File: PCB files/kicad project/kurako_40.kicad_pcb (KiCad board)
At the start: 2 copper layers, 226 x 76.5 mm, 114 parts, among them J1 conn, P1 USB_C_Plug_USB2.0, SW1 TAB, SW10 S, SW11 X, SW12 PROG, SW13 E, SW14 D, SW15 C, SW16 ALT, SW17 R, SW18 F, SW19 V, SW2 ESC, SW20 SPACE, SW21 T, SW22 G, SW23 B, SW24 Y, SW25 H, SW26 N, SW27 LOWER, SW28 U, SW29 J, SW3 SHIFT, SW30 M, SW31 RAISE, SW32 I, SW33 K, SW34 ,, SW35 /, SW36 O, SW37 L, SW38 ., SW39 LEFT, SW4 CTRL, SW40 P, SW41 ;, SW42 UP, SW43 DOWN, SW44 BKSP, SW45 ', SW46 ENTER, SW47 RIGHT, SW48 SW_SPST, SW5 Q, SW6 A, SW7 Z, SW8 WIN, SW9 W, U1 ATmega32U4-AU, Y1 16 Mhz

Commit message: bad keyswitch placements
prior rev had bad switch placement, updated and gave the board a rev number
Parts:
- moved SW42 0.10 mm to (240.0, 108.0)
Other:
- board text added: "kurako_40 Rev 1.1 Nathan Steward"
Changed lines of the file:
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@@
   (general
     (thickness 1.6)
-    (drawings 18)
+    (drawings 19)
     (tracks 1134)
     (zones 0)
@@
     )
   )
-  (module keyswitches:Kailh_socket (layer F.Cu)
+  (module keyswitches:Kailh_socket locked (layer F.Cu)
     (at 126 70 180)
     (descr "MX-style keyswitch with Kailh socket mount")
@@
     )
   )
-  (module keyswitches:Kailh_socket (layer F.Cu)
+  (module keyswitches:Kailh_socket locked (layer F.Cu)
     (at 126 108 180)
     (descr "MX-style keyswitch with Kailh socket mount")
@@
     )
   )
-  (module keyswitches:Kailh_socket (layer F.Cu)
+  (module keyswitches:Kailh_socket locked (layer F.Cu)
     (at 164 70 180)
     (descr "MX-style keyswitch with Kailh socket mount")
@@
     )
   )
-  (module keyswitches:Kailh_socket (layer F.Cu)
+  (module keyswitches:Kailh_socket locked (layer F.Cu)
     (at 202 108 180)
     (descr "MX-style keyswitch with Kailh socket mount")
@@
     )
   )
-  (module keyswitches:Kailh_socket (layer F.Cu)
+  (module keyswitches:Kailh_socket locked (layer F.Cu)
     (at 202 89 180)
     (descr "MX-style keyswitch with Kailh socket mount")
@@
     )
   )
-  (module keyswitches:Kailh_socket (layer F.Cu)
+  (module keyswitches:Kailh_socket locked (layer F.Cu)
     (at 202 70 180)
     (descr "MX-style keyswitch with Kailh socket mount")
@@
     )
   )
-  (module keyswitches:Kailh_socket (layer F.Cu)
+  (module keyswitches:Kailh_socket locked (layer F.Cu)
     (at 183 127 180)
     (descr "MX-style keyswitch with Kailh socket mount")
@@
     )
   )
-  (module keyswitches:Kailh_socket (layer F.Cu)
+  (module keyswitches:Kailh_socket locked (layer F.Cu)
     (at 183 108 180)
     (descr "MX-style keyswitch with Kailh socket mount")
@@
     )
   )
-  (module keyswitches:Kailh_socket (layer F.Cu)
+  (module keyswitches:Kailh_socket locked (layer F.Cu)
     (at 183 89 180)
     (descr "MX-style keyswitch with Kailh socket mount")
@@
     )
   )
-  (module keyswitches:Kailh_socket (layer F.Cu)
+  (module keyswitches:Kailh_socket locked (layer F.Cu)
     (at 183 70 180)
     (descr "MX-style keyswitch with Kailh socket mount")
@@
     )
   )
-  (module keyswitches:Kailh_socket (layer F.Cu)
+  (module keyswitches:Kailh_socket locked (layer F.Cu)
     (at 164 127 180)
     (descr "MX-style keyswitch with Kailh socket mount")
@@
     )
   )
-  (module keyswitches:Kailh_socket (layer F.Cu)
+  (module keyswitches:Kailh_socket locked (layer F.Cu)
     (at 164 108 180)
     (descr "MX-style keyswitch with Kailh socket mount")
@@
     )
   )
-  (module keyswitches:Kailh_socket (layer F.Cu)
+  (module keyswitches:Kailh_socket locked (layer F.Cu)
     (at 145 108 180)
     (descr "MX-style keyswitch with Kailh socket mount")
@@
     )
   )
-  (module keyswitches:Kailh_socket (layer F.Cu)
+  (module keyswitches:Kailh_socket locked (layer F.Cu)
     (at 202 127 180)
     (descr "MX-style keyswitch with Kailh socket mount")
@@
     )
   )
-  (module keyswitches:Kailh_socket (layer F.Cu)
+  (module keyswitches:Kailh_socket locked (layer F.Cu)
     (at 221 108 180)
     (descr "MX-style keyswitch with Kailh socket mount")
@@
     )
   )
-  (module keyswitches:Kailh_socket (layer F.Cu)
+  (module keyswitches:Kailh_socket locked (layer F.Cu)
     (at 221 127 180)
     (descr "MX-style keyswitch with Kailh socket mount")
@@
     )
   )
-  (module keyswitches:Kailh_socket (layer F.Cu)
+  (module keyswitches:Kailh_socket locked (layer F.Cu)
     (at 240 70 180)
     (descr "MX-style keyswitch with Kailh socket mount")
@@
     )
   )
-  (module keyswitches:Kailh_socket (layer F.Cu)
+  (module keyswitches:Kailh_socket locked (layer F.Cu)
     (at 240 89 180)
     (descr "MX-style keyswitch with Kailh socket mount")
@@
     )
   )
-  (module keyswitches:Kailh_socket (layer F.Cu)
-    (at 240 108.1 180)
+  (module keyswitches:Kailh_socket locked (layer F.Cu)
+    (at 240 108 180)
     (descr "MX-style keyswitch with Kailh socket mount")
     (tags MX,cherry,gateron,kailh,pg1511,socket)
@@
     )
   )
-  (module keyswitches:Kailh_socket (layer F.Cu)
+  (module keyswitches:Kailh_socket locked (layer F.Cu)
     (at 240 127 180)
     (descr "MX-style keyswitch with Kailh socket mount")
@@
     )
   )
-  (module keyswitches:Kailh_socket (layer F.Cu)
+  (module keyswitches:Kailh_socket locked (layer F.Cu)
     (at 259 70 180)
     (descr "MX-style keyswitch with Kailh socket mount")
@@
     )
   )
-  (module keyswitches:Kailh_socket (layer F.Cu)
+  (module keyswitches:Kailh_socket locked (layer F.Cu)
     (at 259 89 180)
     (descr "MX-style keyswitch with Kailh socket mount")
@@
     )
   )
-  (module keyswitches:Kailh_socket (layer F.Cu)
+  (module keyswitches:Kailh_socket locked (layer F.Cu)
     (at 259 108 180)
     (descr "MX-style keyswitch with Kailh socket mount")
@@
     )
   )
-  (module keyswitches:Kailh_socket (layer F.Cu)
+  (module keyswitches:Kailh_socket locked (layer F.Cu)
     (at 259 127 180)
     (descr "MX-style keyswitch with Kailh socket mount")
@@
     )
   )
-  (module keyswitches:Kailh_socket (layer F.Cu)
+  (module keyswitches:Kailh_socket locked (layer F.Cu)
     (at 88 127 180)
     (descr "MX-style keyswitch with Kailh socket mount")
@@
     )
   )
-  (module keyswitches:Kailh_socket (layer F.Cu)
+  (module keyswitches:Kailh_socket locked (layer F.Cu)
     (at 221 70 180)
     (descr "MX-style keyswitch with Kailh socket mount")
@@
     )
   )
-  (module keyswitches:Kailh_socket (layer F.Cu)
+  (module keyswitches:Kailh_socket locked (layer F.Cu)
     (at 88 89 180)
     (descr "MX-style keyswitch with Kailh socket mount")
@@
     )
   )
-  (module keyswitches:Kailh_socket (layer F.Cu)
+  (module keyswitches:Kailh_socket locked (layer F.Cu)
     (at 88 70 180)
     (descr "MX-style keyswitch with Kailh socket mount")
@@
     )
   )
-  (module keyswitches:Kailh_socket (layer F.Cu)
+  (module keyswitches:Kailh_socket locked (layer F.Cu)
     (at 69 127 180)
     (descr "MX-style keyswitch with Kailh socket mount")
@@
     )
   )
-  (module keyswitches:Kailh_socket (layer F.Cu)
+  (module keyswitches:Kailh_socket locked (layer F.Cu)
     (at 69 108 180)
     (descr "MX-style keyswitch with Kailh socket mount")
@@
     )
   )
-  (module keyswitches:Kailh_socket (layer F.Cu)
+  (module keyswitches:Kailh_socket locked (layer F.Cu)
     (at 69 89 180)
     (descr "MX-style keyswitch with Kailh socket mount")
@@
     )
   )
-  (module keyswitches:Kailh_socket (layer F.Cu)
+  (module keyswitches:Kailh_socket locked (layer F.Cu)
     (at 69 70 180)
     (descr "MX-style keyswitch with Kailh socket mount")
@@
     )
   )
-  (module keyswitches:Kailh_socket (layer F.Cu)
+  (module keyswitches:Kailh_socket locked (layer F.Cu)
     (at 50 127 180)
     (descr "MX-style keyswitch with Kailh socket mount")
@@
     )
   )
-  (module keyswitches:Kailh_socket (layer F.Cu)
+  (module keyswitches:Kailh_socket locked (layer F.Cu)
     (at 50 108 180)
     (descr "MX-style keyswitch with Kailh socket mount")
@@
     )
   )
-  (module keyswitches:Kailh_socket (layer F.Cu)
+  (module keyswitches:Kailh_socket locked (layer F.Cu)
     (at 50 89 180)
     (descr "MX-style keyswitch with Kailh socket mount")
@@
     )
   )
-  (module keyswitches:Kailh_socket (layer F.Cu)
+  (module keyswitches:Kailh_socket locked (layer F.Cu)
     (at 164 89 180)
     (descr "MX-style keyswitch with Kailh socket mount")
@@
     )
   )
-  (module keyswitches:Kailh_socket (layer F.Cu)
+  (module keyswitches:Kailh_socket locked (layer F.Cu)
     (at 107 70 180)
     (descr "MX-style keyswitch with Kailh socket mount")
@@
     )
   )
-  (module keyswitches:Kailh_socket (layer F.Cu)
+  (module keyswitches:Kailh_socket locked (layer F.Cu)
     (at 107 89 180)
     (descr "MX-style keyswitch with Kailh socket mount")
@@
     )
   )
-  (module keyswitches:Kailh_socket (layer F.Cu)
+  (module keyswitches:Kailh_socket locked (layer F.Cu)
     (at 107 108)
     (descr "MX-style keyswitch with Kailh socket mount")
@@
     )
   )
-  (module keyswitches:Kailh_socket (layer F.Cu)
+  (module keyswitches:Kailh_socket locked (layer F.Cu)
     (at 107 127 180)
     (descr "MX-style keyswitch with Kailh socket mount")
@@
     )
   )
-  (module keyswitches:Kailh_socket (layer F.Cu)
+  (module keyswitches:Kailh_socket locked (layer F.Cu)
     (at 126 89 180)
     (descr "MX-style keyswitch with Kailh socket mount")
@@
     )
   )
-  (module keyswitches:Kailh_socket (layer F.Cu)
+  (module keyswitches:Kailh_socket locked (layer F.Cu)
     (at 135.5 127 180)
     (descr "MX-style keyswitch with Kailh socket mount")
@@
     )
   )
-  (module keyswitches:Kailh_socket (layer F.Cu)
+  (module keyswitches:Kailh_socket locked (layer F.Cu)
     (at 145 70 180)
     (descr "MX-style keyswitch with Kailh socket mount")
@@
     )
   )
-  (module keyswitches:Kailh_socket (layer F.Cu)
+  (module keyswitches:Kailh_socket locked (layer F.Cu)
     (at 145 89 180)
     (descr "MX-style keyswitch with Kailh socket mount")
@@
     )
   )
-  (module keyswitches:Kailh_socket (layer F.Cu)
+  (module keyswitches:Kailh_socket locked (layer F.Cu)
     (at 221 89 180)
     (descr "MX-style keyswitch with Kailh socket mount")
@@
     )
   )
-  (module keyswitches:Kailh_socket (layer F.Cu)
+  (module keyswitches:Kailh_socket locked (layer F.Cu)
     (at 88 108)
     (descr "MX-style keyswitch with Kailh socket mount")
@@
     )
   )
-  (module Connector_USB:USB_C_Receptacle_Amphenol_12401610E4-2A (layer B.Cu)
+  (module Connector_USB:USB_C_Receptacle_Amphenol_12401610E4-2A locked (layer B.Cu)
     (at 78.5 62.5)
     (descr "USB TYPE C, RA RCPT PCB, SMT, https://www.amphenolcanada.com/StockAvailabilityPrice.aspx?From=&PartNum=12401610E4%7e2A")
@@
     (pad "" np_thru_hole circle (at -11.9 6.985) (size 3.048 3.048) (drill 3.048) (layers *.Cu *.Mask))
   )
+  (gr_text "kurako_40 Rev 1.1\nNathan Steward" (at 59.5 65) (layer B.SilkS)
+    (effects (font (size 1.5 1.5) (thickness 0.3)) (justify mirror))
+  )
   (gr_text SCK (at 62.25 101.25) (layer B.SilkS)

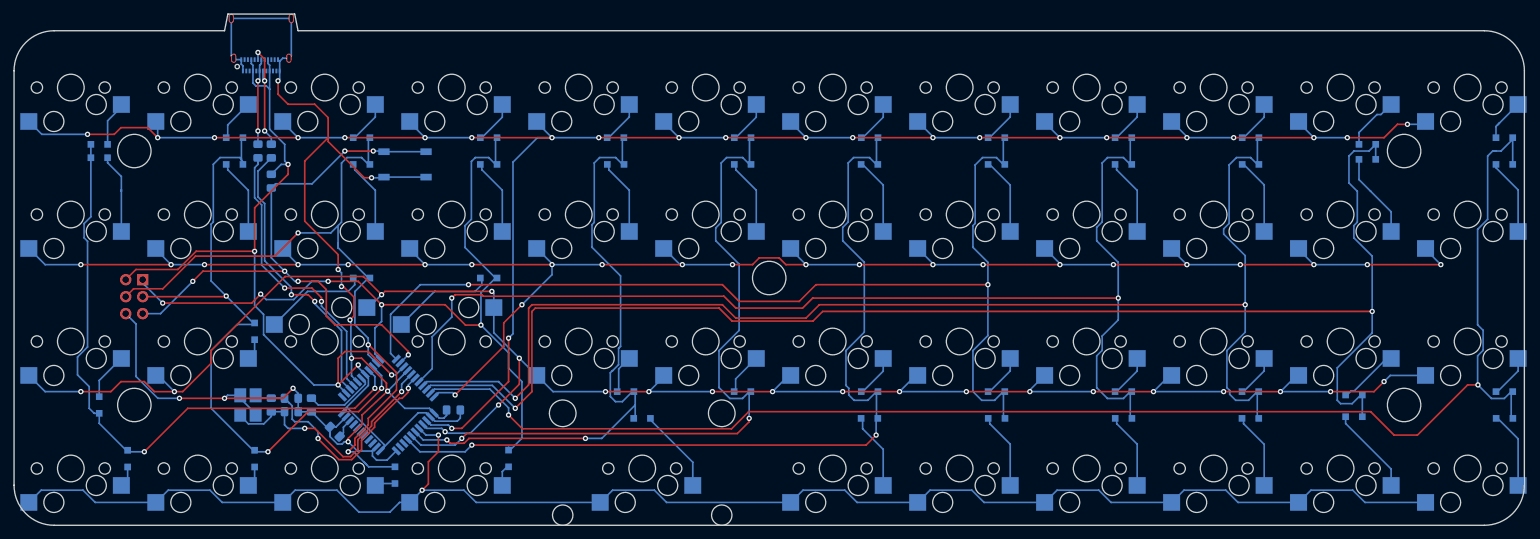
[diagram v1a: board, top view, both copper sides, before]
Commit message: board rev changes v1.2
updated schematic from SOD323 diodes to SOD80 due to cost savings and ease of soldering. added ground fill on top and bottom
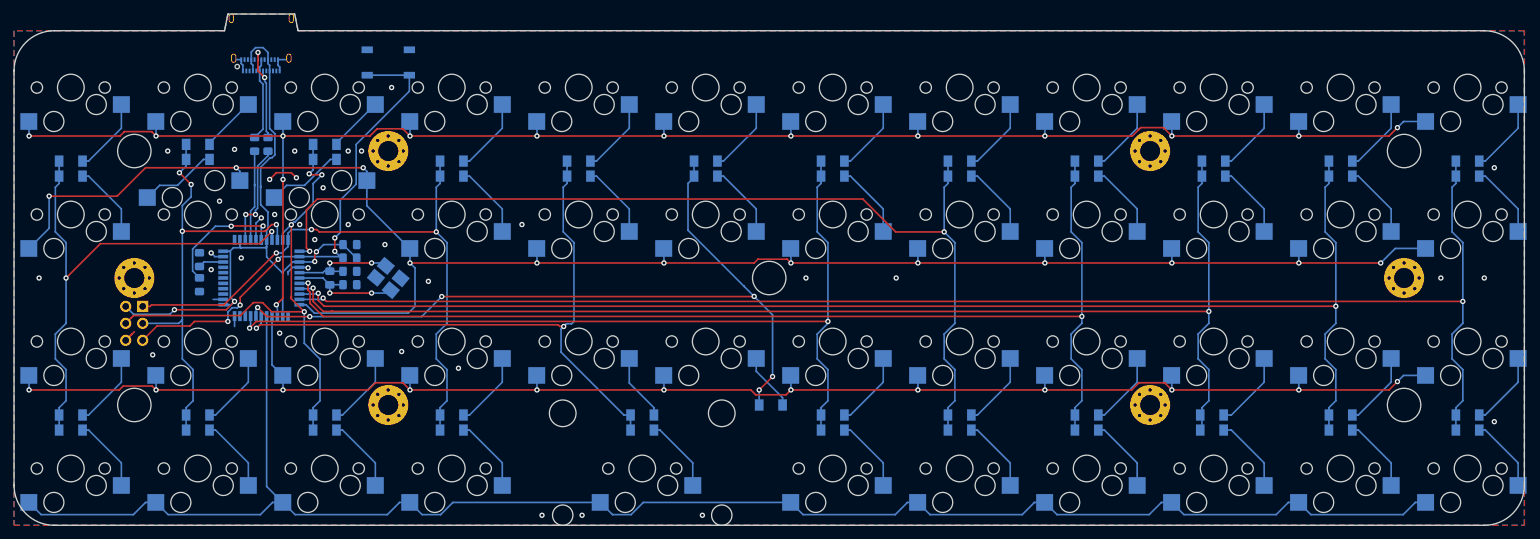
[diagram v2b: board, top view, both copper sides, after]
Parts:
- added ?: MountingHole_3mm_Pad_Via, MountingHole:MountingHole_3mm_Pad_Via, F.Cu at (249.5, 98.5)
- added ?: MountingHole_3mm_Pad_Via, MountingHole:MountingHole_3mm_Pad_Via, F.Cu at (211.5, 117.5)
- added ?: MountingHole_3mm_Pad_Via, MountingHole:MountingHole_3mm_Pad_Via, F.Cu at (211.5, 79.5)
- added ?: MountingHole_3mm_Pad_Via, MountingHole:MountingHole_3mm_Pad_Via, F.Cu at (97.5, 117.5)
- added ?: MountingHole_3mm_Pad_Via, MountingHole:MountingHole_3mm_Pad_Via, F.Cu at (97.5, 79.5)
- added ?: MountingHole_3mm_Pad_Via, MountingHole:MountingHole_3mm_Pad_Via, F.Cu at (59.5, 98.5)
- added G***: LOGO, silkscreen library:pjmeme_edit, B.Cu at (233.0, 98.4)
- D1, D10, D11, D12, D13, D14, D15, D16, D17, D18, D19, D2, D20, D21, D22, D23, D24, D25, D26, D27, D28, D29, D3, D30, D31, D32, D33, D34, D35, D36, D37, D38, D39, D4, D40, D41, D42, D43, D44, D45, D46, D47, D5, D6, D7, D8, D9: footprint Diode_SMD:D_SOD-323_HandSoldering -> Diode_SMD:D_MiniMELF
- moved C1 32.8 mm to (69.2, 95.8), turned to 90 degrees
- moved C5 29.2 mm to (91.8, 93.5), turned to 0 degrees
- moved Y1 28.3 mm to (97.5, 98.5), turned to 140 degrees
- moved U1 26.9 mm to (78.5, 98.5), turned to 270 degrees
- moved C2 24.6 mm to (69.2, 99.5)
- moved C4 22.8 mm to (91.8, 97.5)
- moved D15 21.2 mm to (107.0, 119.0), turned to 0 degrees
- moved D11 21.2 mm to (88.0, 119.0), turned to 0 degrees
- moved R4 20.9 mm to (88.8, 98.5), turned to 90 degrees
- moved C3 19.1 mm to (91.8, 99.5)
- moved R3 16.4 mm to (91.8, 95.5), turned to 180 degrees
- moved SW48 15.5 mm to (97.5, 66.2), turned to 180 degrees
- moved D7 15.1 mm to (69.0, 119.0), turned to 0 degrees
- moved D12 12.5 mm to (88.0, 121.2), turned to 0 degrees
- moved D4 9.51 mm to (50.0, 121.2), turned to 0 degrees
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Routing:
- net GND: track 208.3 -> 26.8 mm, vias 11 -> 37
- net VBUS: track 147.0 -> 99.5 mm, vias 5 -> 4
- net ROW00: track 300.8 -> 264.5 mm, vias 24 -> 14
- net ROW02: track 281.7 -> 246.3 mm, vias 21 -> 12
- net COL01: track 100.9 -> 68.5 mm, vias 3 -> 4
- net COL03: track 124.9 -> 92.9 mm, vias 5 -> 3
- net D+: track 43.5 -> 13.8 mm, vias 2 -> 0
- net COL02: track 109.0 -> 80.6 mm, vias 3 -> 4
- net D-: track 42.7 -> 15.5 mm
- net X2: track 38.3 -> 16.4 mm
- net X1: track 36.6 -> 17.5 mm
- net COL00: track 94.8 -> 77.8 mm
- net ROW03: track 237.9 -> 253.0 mm, vias 2 -> 0
- net RST: track 90.7 -> 75.7 mm, vias 6 -> 5
- net COL10: track 212.9 -> 199.7 mm
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- added copper zone on B.Cu, net GND
- added copper zone on F.Cu, net GND
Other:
- board text added: "kurako_40 Rev 1.2 Nathan Steward"
- board text removed: "GND"
- board text removed: "MISO"
- board text removed: "MOSI"
- board text removed: "RST"
- board text removed: "SCK"
- board text removed: "VCC"
- board text removed: "kurako_40 Rev 1.1 Nathan Steward"

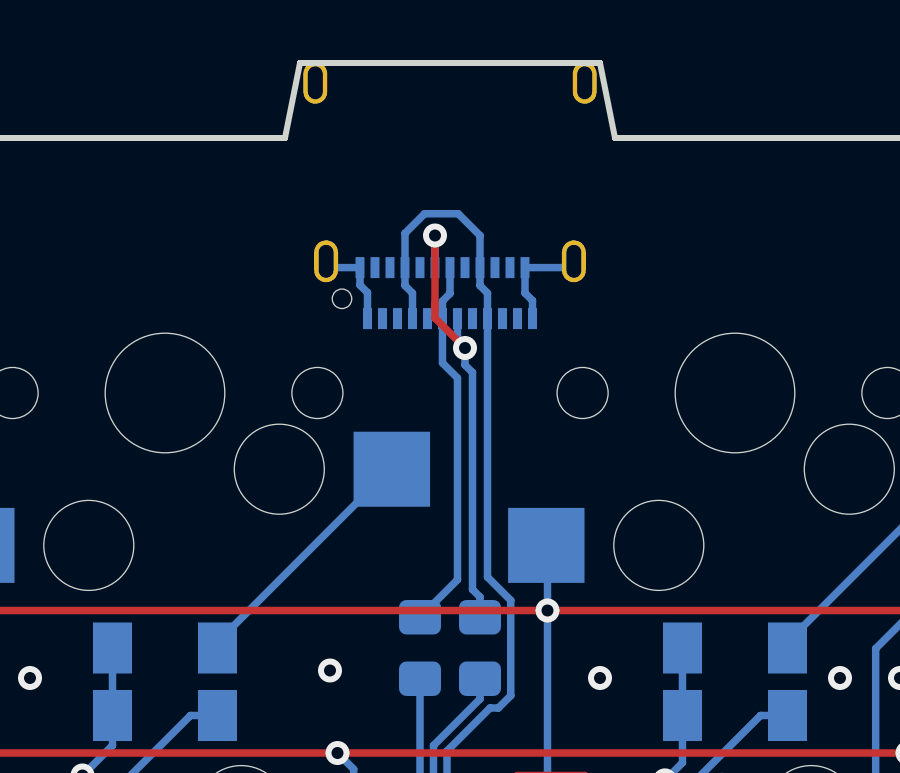
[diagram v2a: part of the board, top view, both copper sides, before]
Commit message: minor board and code change
updated usb placement to not stick out as much (-0.75mm)
swapped diode polarity in firmware config
corrected main board header file
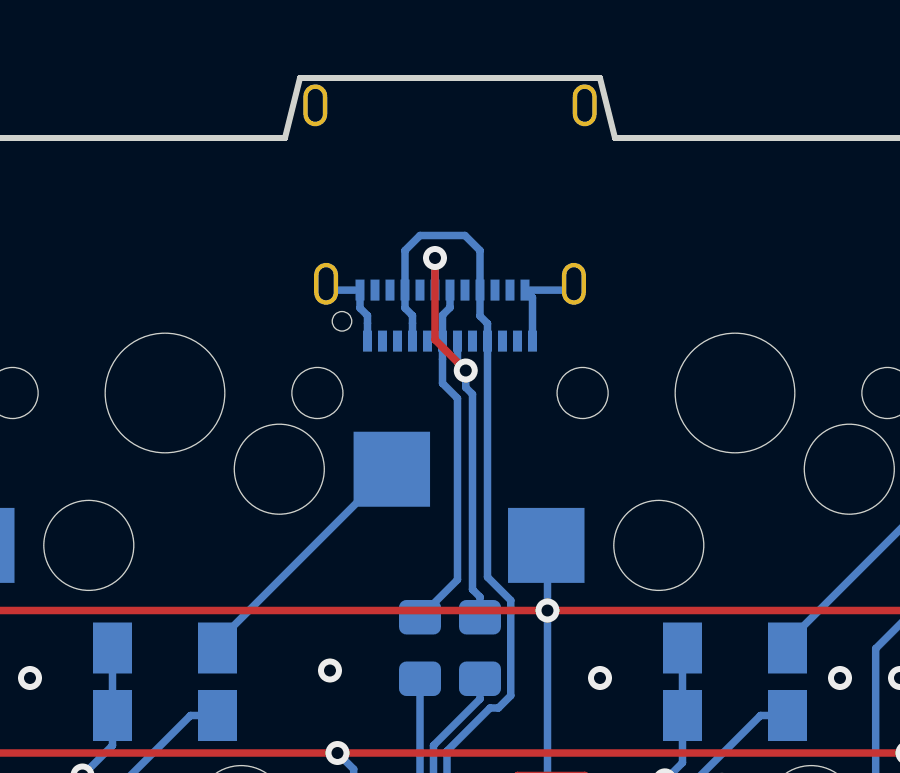
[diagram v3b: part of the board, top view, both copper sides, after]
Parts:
- moved P1 0.75 mm to (78.5, 63.2)
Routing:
- net Net-(P1-PadA7): track 15.7 -> 14.8 mm
- net Net-(P1-PadA6): track 12.5 -> 11.7 mm
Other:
- board size 226 x 76.5 mm -> 226 x 76 mm
- board text added: "kurako_40 Rev 1.3 Nathan Steward"
- board text removed: "kurako_40 Rev 1.2 Nathan Steward"
